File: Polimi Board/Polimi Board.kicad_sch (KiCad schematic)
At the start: 19 parts, among them SW1 MCU Reset, SW8 SW_Push, U1 STM32F205RCTx, Y1 25MHz

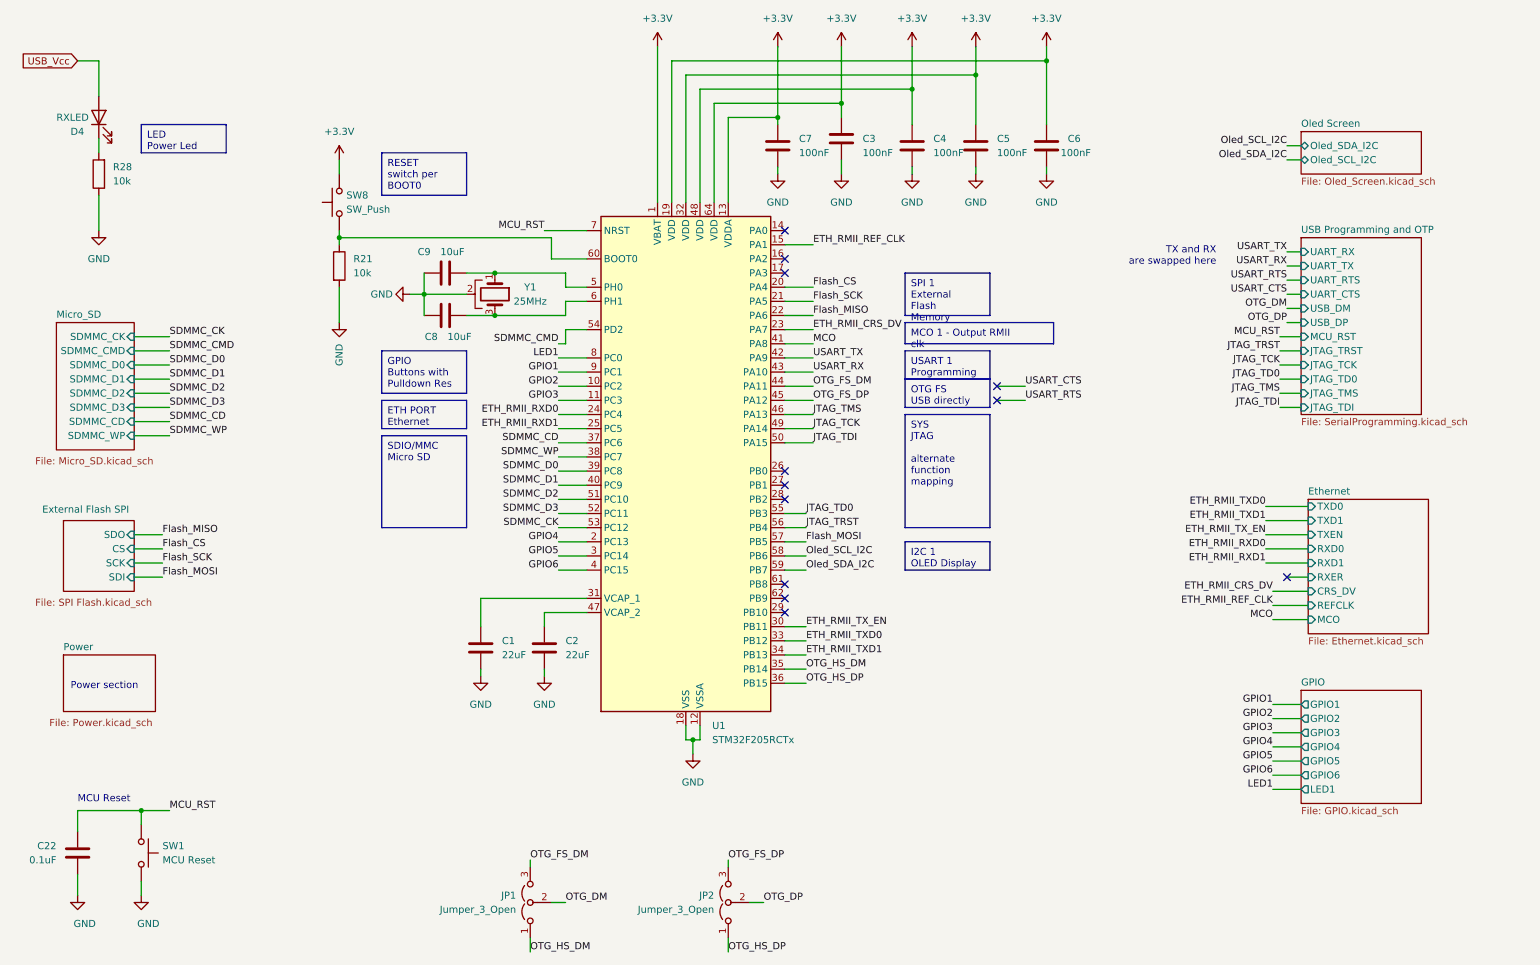
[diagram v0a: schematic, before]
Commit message: Added footprint from Mouser
readu for wiring
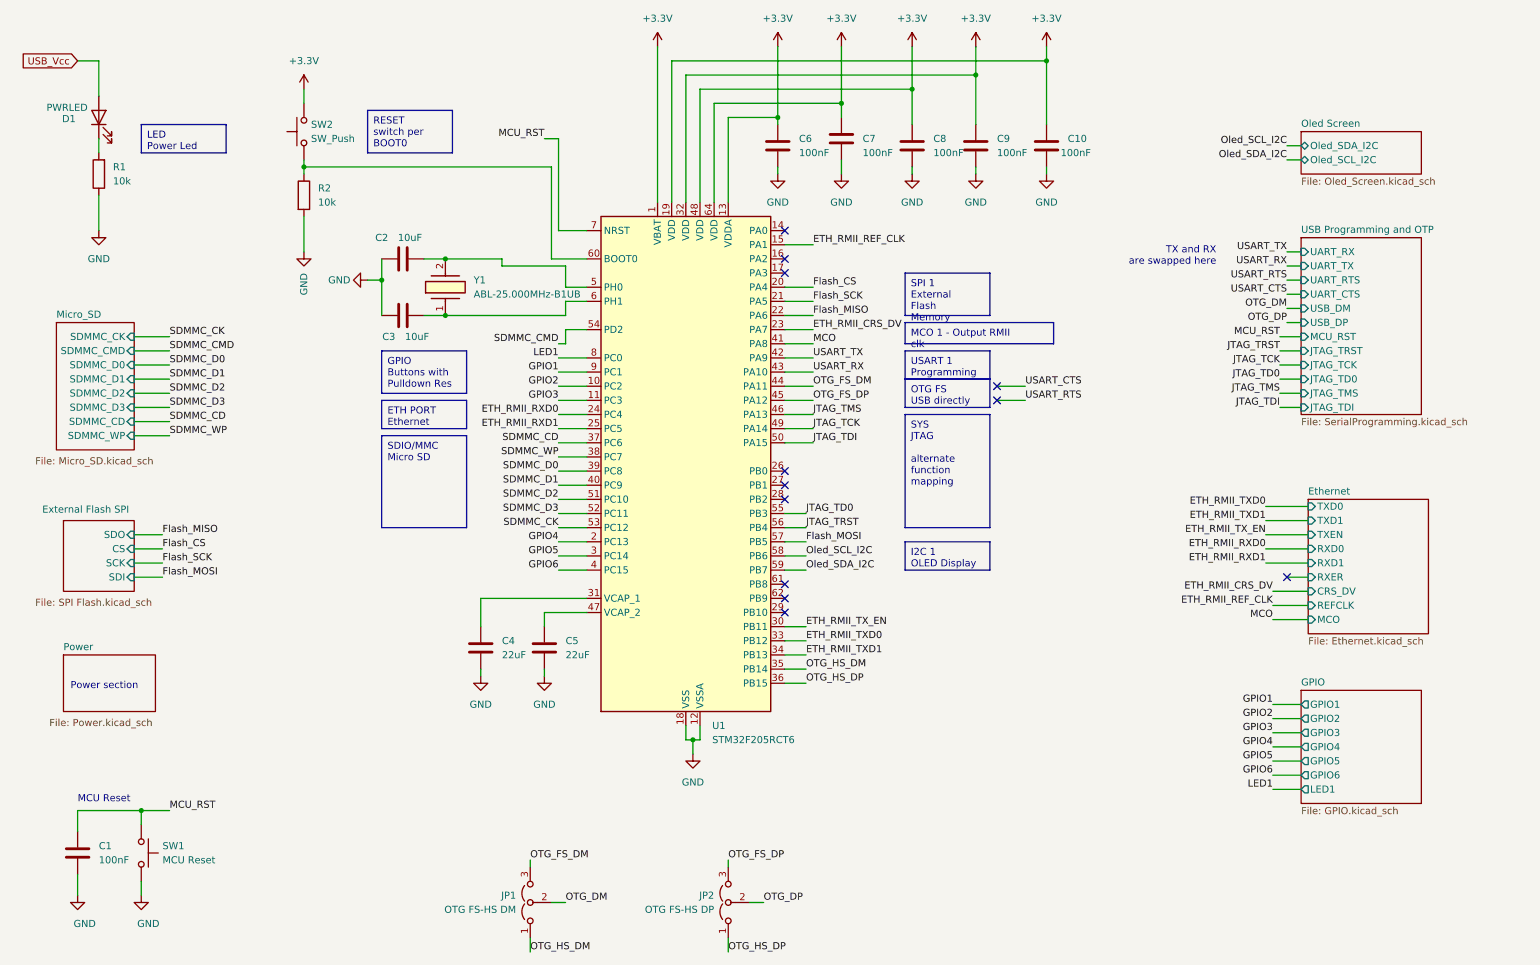
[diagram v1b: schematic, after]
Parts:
- removed Y1: 25MHz, symbol Device:Crystal_GND2
- added Y1: ABL-25.000MHz-B1UB, SamacSys_Parts:ABL25000MHzB1UB, symbol SamacSys_Parts:ABL-25.000MHz-B1UB
- C1: renamed from C22; value 0.1uF -> 100nF; footprint (none) -> Capacitor_SMD:C_0603_1608Metric_Pad1.08x0.95mm_HandSolder
- C10: renamed from C6; footprint (none) -> Capacitor_SMD:C_0603_1608Metric_Pad1.08x0.95mm_HandSolder
- C2: renamed from C9; footprint (none) -> Capacitor_SMD:C_0603_1608Metric_Pad1.08x0.95mm_HandSolder
- C3: renamed from C8; footprint (none) -> Capacitor_SMD:C_0603_1608Metric_Pad1.08x0.95mm_HandSolder
- C4: renamed from C1; footprint (none) -> Capacitor_SMD:C_0603_1608Metric_Pad1.08x0.95mm_HandSolder
- C5: renamed from C2; footprint (none) -> Capacitor_SMD:C_0603_1608Metric_Pad1.08x0.95mm_HandSolder
- C6: renamed from C7; footprint (none) -> Capacitor_SMD:C_0603_1608Metric_Pad1.08x0.95mm_HandSolder
- C7: renamed from C3; footprint (none) -> Capacitor_SMD:C_0603_1608Metric_Pad1.08x0.95mm_HandSolder
- C8: renamed from C4; footprint (none) -> Capacitor_SMD:C_0603_1608Metric_Pad1.08x0.95mm_HandSolder
- C9: renamed from C5; footprint (none) -> Capacitor_SMD:C_0603_1608Metric_Pad1.08x0.95mm_HandSolder
- D1: renamed from D4; value RXLED -> PWRLED; footprint (none) -> LED_THT:LED_D3.0mm
- JP1: value Jumper_3_Open -> OTG FS-HS DM; footprint (none) -> Connector_PinHeader_2.54mm:PinHeader_1x03_P2.54mm_Vertical
- JP2: value Jumper_3_Open -> OTG FS-HS DP; footprint (none) -> Connector_PinHeader_2.54mm:PinHeader_1x03_P2.54mm_Vertical
- R1: renamed from R28; footprint (none) -> Resistor_SMD:R_0603_1608Metric_Pad0.98x0.95mm_HandSolder
- R2: renamed from R21; footprint (none) -> Resistor_SMD:R_0603_1608Metric_Pad0.98x0.95mm_HandSolder
- SW1: footprint (none) -> Button_Switch_THT:SW_PUSH_6mm_H5mm
- SW2: renamed from SW8; footprint (none) -> Button_Switch_THT:SW_PUSH_6mm_H5mm
- U1: value STM32F205RCTx -> STM32F205RCT6
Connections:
- net at C2.1, U1.5 (PH0): now also Y1.2
- net at C3.1, U1.6 (PH1): now also Y1.1
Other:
- moved on the sheet: C2, C3, R2, SW2

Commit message: PCB wip
before holidays
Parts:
- SW2: value SW_Push -> Boot
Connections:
- net GPIO_EXT_1: now reaches U1.14 (PA0)
- net GPIO_EXT_2: now reaches U1.16 (PA2)
- net GPIO_EXT_3: now reaches U1.17 (PA3)
- net GPIO_EXT_4: now reaches U1.26 (PB0)
- net GPIO_EXT_5: now reaches U1.27 (PB1)
- net GPIO_EXT_6: now reaches U1.28 (PB2)
- net GPIO_EXT_9: now reaches U1.29 (PB10)
- net GPIO_EXT_7: now reaches U1.61 (PB8)
- net GPIO_EXT_8: now reaches U1.62 (PB9)
- net SDMMC_WP renamed GPIO_EXT_10
- no-connect marks 12 -> 3
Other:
- sheet GPIO ports: added GPIO_EXT_1, GPIO_EXT_10, GPIO_EXT_2, GPIO_EXT_3, GPIO_EXT_4, GPIO_EXT_5, GPIO_EXT_6, GPIO_EXT_7, GPIO_EXT_8, GPIO_EXT_9; removed none
- sheet Micro_SD ports: added none; removed SDMMC_WP

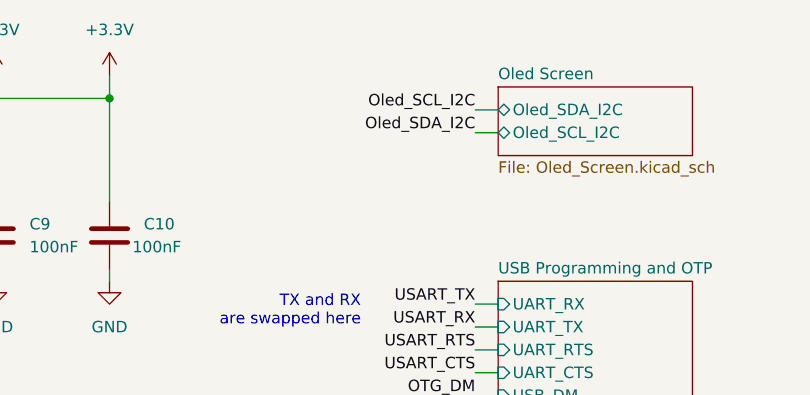
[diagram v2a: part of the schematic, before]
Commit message: Solved issues
3.3V 3V3 and others
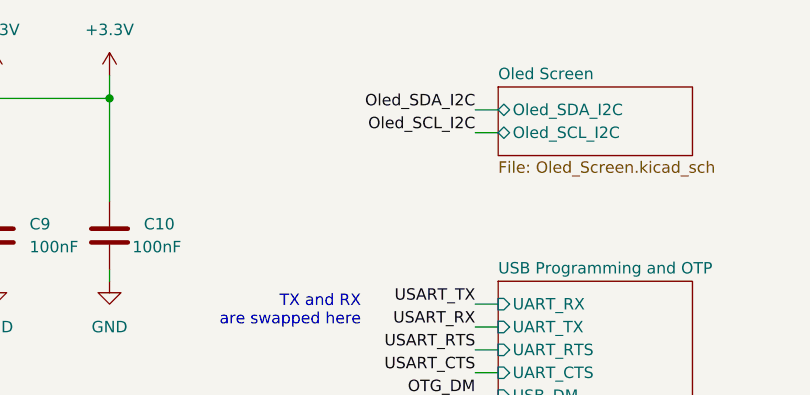
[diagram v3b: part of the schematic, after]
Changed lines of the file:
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@@
 	(title_block
 		(title "Polimi Board ")
-		(date "2024-07-16")
+		(date "2024-09-11")
 		(rev "2.0")
 		(company "Politecnico di Milano")
@@
 	(wire
 		(pts
+			(xy 245.11 29.21) (xy 247.65 29.21)
+		)
+		(stroke
+			(width 0)
+			(type default)
+		)
+	)
+	(wire
+		(pts
 			(xy 116.84 93.98) (xy 121.92 93.98)
 		)
@@
 	(wire
 		(pts
+			(xy 245.11 31.75) (xy 247.65 31.75)
+		)
+		(stroke
+			(width 0)
+			(type default)
+		)
+	)
+	(wire
+		(pts
 			(xy 195.58 88.9) (xy 200.66 88.9)
 		)
@@
 	(wire
 		(pts
-			(xy 245.11 31.75) (xy 247.65 31.75)
-		)
-		(stroke
-			(width 0)
-			(type default)
-		)
-	)
-	(wire
-		(pts
 			(xy 71.12 46.99) (xy 115.57 46.99)
 		)
@@
 		(pts
 			(xy 142.24 33.02) (xy 180.34 33.02)
-		)
-		(stroke
-			(width 0)
-			(type default)
-		)
-	)
-	(wire
-		(pts
-			(xy 245.11 29.21) (xy 247.65 29.21)
 		)
 		(stroke
@@
 	)
 	(label "Oled_SCL_I2C"
-		(at 245.11 29.21 180)
+		(at 245.11 31.75 180)
 		(fields_autoplaced yes)
 		(effects
@@
 	)
 	(label "Oled_SDA_I2C"
-		(at 245.11 31.75 180)
-		(fields_autoplaced yes)
-		(effects
+		(at 245.11 29.21 180)
+		(fields_autoplaced yes)
+		(effects
